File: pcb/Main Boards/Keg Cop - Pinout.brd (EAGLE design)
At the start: 51.3 x 51 mm, 28 parts

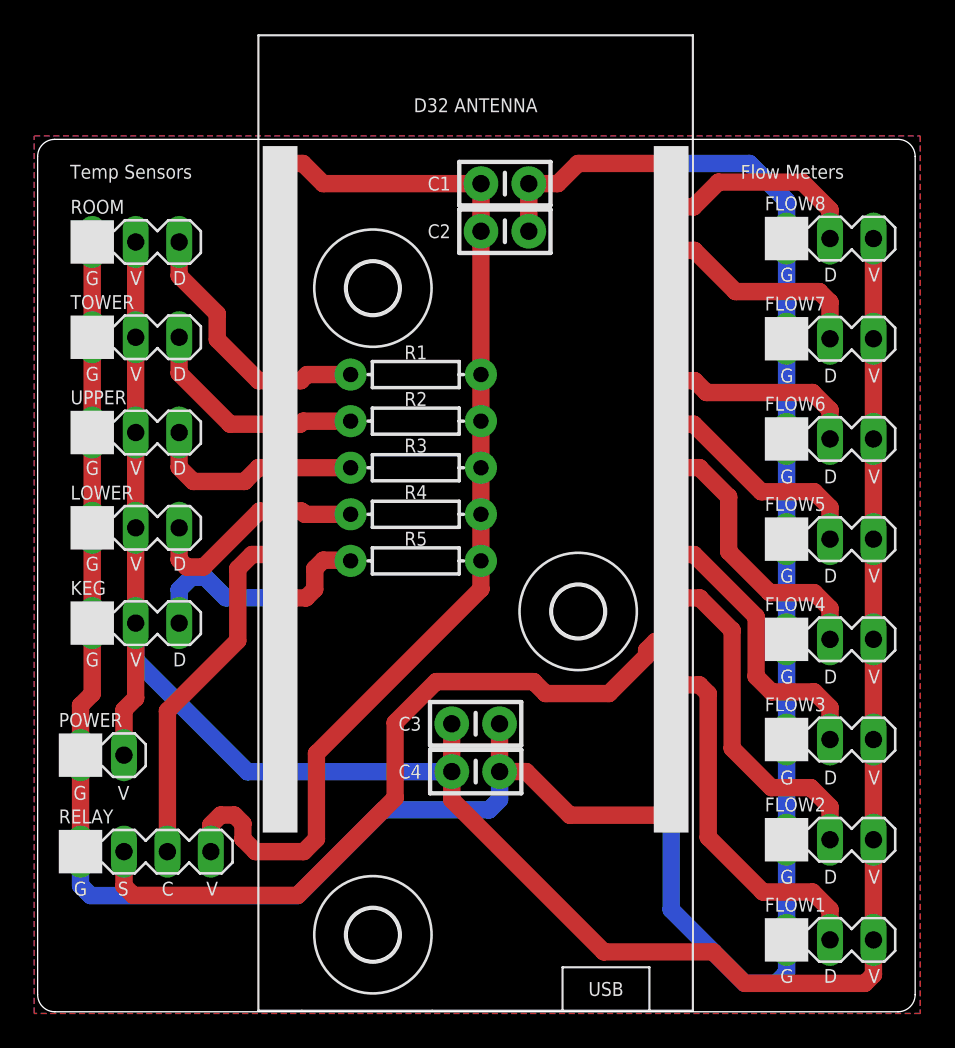
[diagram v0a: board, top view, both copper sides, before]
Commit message: Renamed files
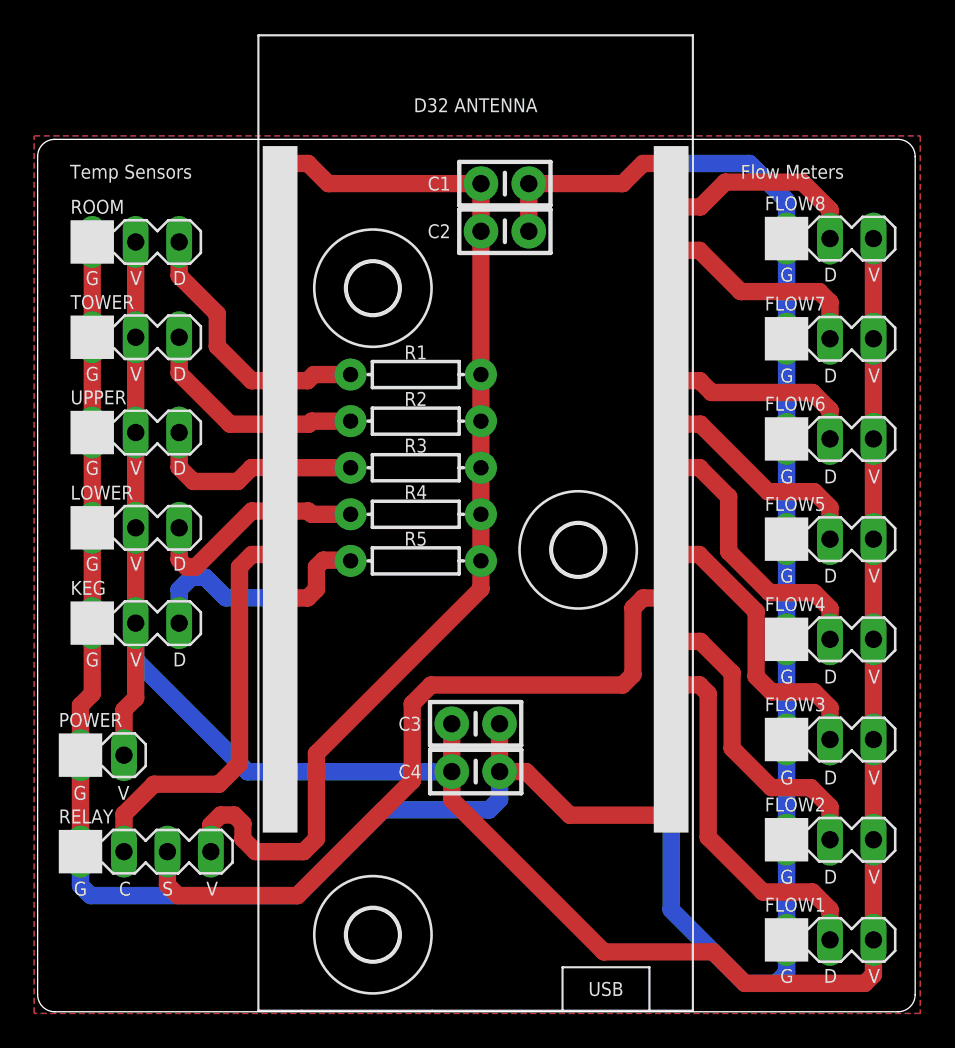
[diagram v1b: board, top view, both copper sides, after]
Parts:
- moved U$3 3.60 mm to (31.6, 27.0)
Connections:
- net COOL: now also RELAY.2; no longer RELAY.3
- net KEG2: now also D32.IO4; no longer D32.IO16
- net SOL: now also D32.IO16, RELAY.3; no longer D32.IO4, RELAY.2
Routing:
- net COOL: track 21.1 -> 24.3 mm
- net KEG2: track 20.3 -> 17.8 mm
